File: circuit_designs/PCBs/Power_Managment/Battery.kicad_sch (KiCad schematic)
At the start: 20 parts, among them J1 Conn_01x02_Pin, J2 Conn_01x02_Pin, J3 Conn_01x02_Pin, U1 LM2596T-ADJ, U2 LM2596T-ADJ

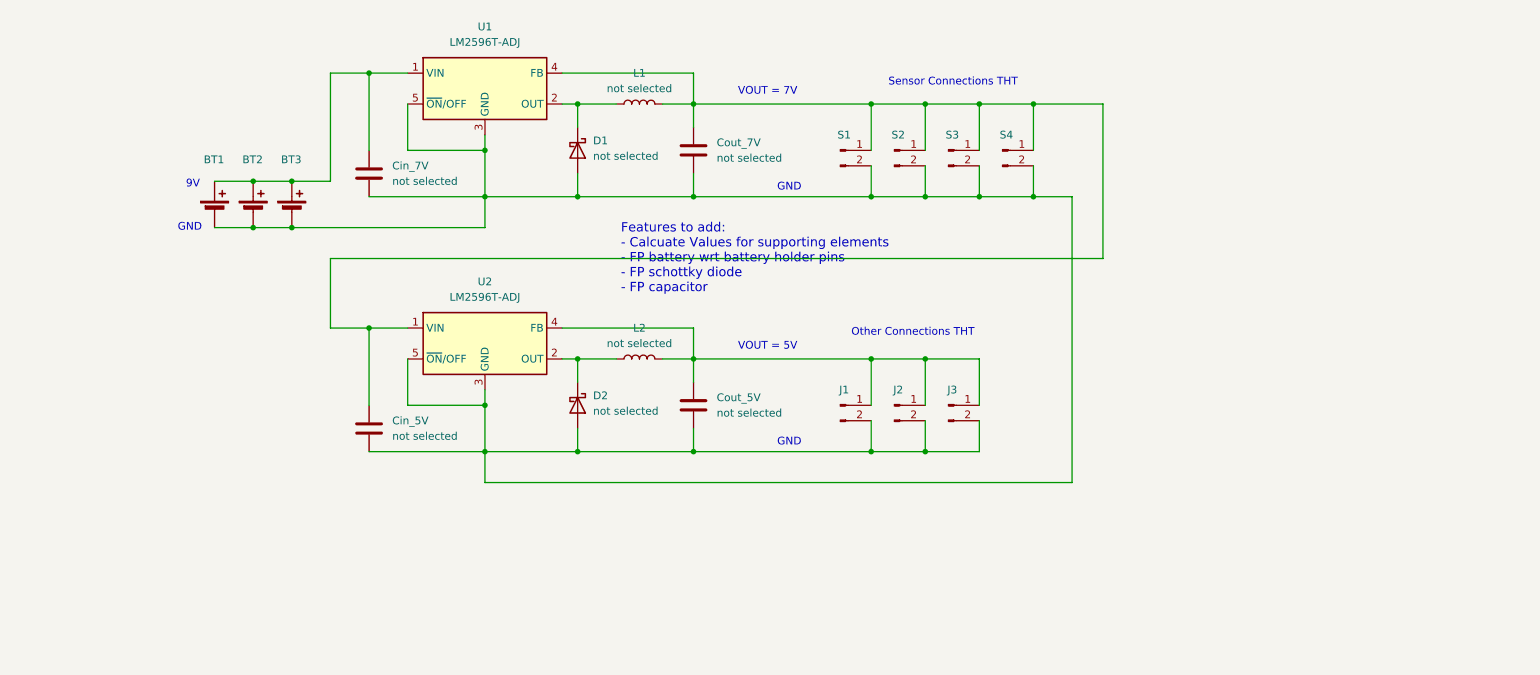
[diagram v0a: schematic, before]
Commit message: adam's and emmanuel's updates on the power management circuit - added values for the electronics (caps, inducts...) and added buzzer EPS
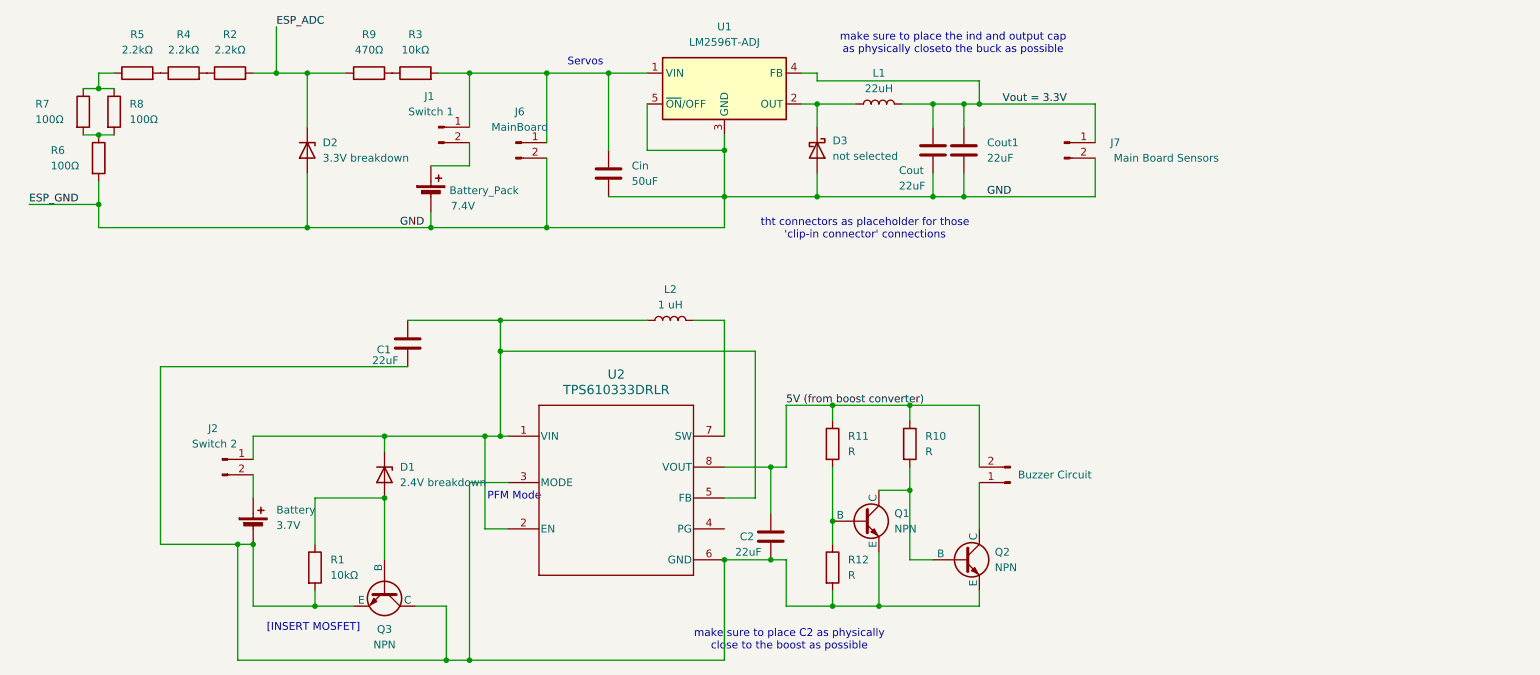
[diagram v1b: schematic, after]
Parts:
- removed BT1, BT2, BT3: 9V, symbol Device:Battery_Cell
- removed Cin_5V, Cin_7V, Cout_5V, Cout_7V: not selected, symbol Device:C
- removed D1, D2: not selected, symbol Device:D_Schottky
- removed S1, S2, S3, S4: Conn_01x02_Pin, mylibrary:External_Connection_2pin, symbol Connector:Conn_01x02_Pin
- removed U2: LM2596T-ADJ, Package_TO_SOT_THT:TO-220-5_P3.4x3.7mm_StaggerOdd_Lead3.8mm_Vertical, symbol Regulator_Switching:LM2596T-ADJ
- added Battery: 3.7V, symbol Device:Battery_Cell
- added Battery_Pack: 7.4V, symbol Device:Battery_Cell
- added C1, C2, Cout, Cout1: 22uF, symbol Device:C
- added Cin: 50uF, symbol Device:C
- added D1: 2.4V breakdown, Diode_THT:D_DO-41_SOD81_P10.16mm_Horizontal, symbol Diode:1N47xxA
- added D2: 3.3V breakdown, Diode_THT:D_DO-41_SOD81_P10.16mm_Horizontal, symbol Diode:1N47xxA
- added D3: not selected, symbol Device:D_Schottky
- added J6: MainBoard, symbol Connector:Conn_01x02_Pin
- added J7: Main Board Sensors, symbol Connector:Conn_01x02_Pin
- added Q1, Q2, Q3: NPN, symbol Simulation_SPICE:NPN
- added R1, R3: 10kΩ, symbol Device:R
- added R10, R11, R12: R, symbol Device:R
- added R2, R4, R5: 2.2kΩ, symbol Device:R
- added R6, R7, R8: 100Ω, symbol Device:R
- added R9: 470Ω, symbol Device:R
- added U2: TPS610333DRLR, mylibrary:TPS610333, symbol Project_Library:TPS610333DRLR
- J1: value Conn_01x02_Pin -> Switch 1; footprint mylibrary:External_Connection_2pin -> (none)
- J2: value Conn_01x02_Pin -> Switch 2; footprint mylibrary:External_Connection_2pin -> (none)
- J3: value Conn_01x02_Pin -> Buzzer Circuit; footprint mylibrary:External_Connection_2pin -> (none)
- L1: value not selected -> 22uH
- L2: value not selected -> 1 uH
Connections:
- net Vout = 3.3V: now reaches L1.2, U1.4 (FB)
- net Vout = 3.3V: now also Cout.1, Cout1.1, J7.1 (Pin_1)
- net at U1.1 (VIN): now also J1.1 (Pin_1), Cin.1, J6.1 (Pin_1), R3.2
- net at L2.1: now also J2.1 (Pin_1), C1.1, D1.1 (K), U2.1 (VIN), U2.2 (EN), U2.5 (FB)
- net at L1.1, U1.2 (OUT): now also D3.1 (K)
- new net: Battery.2 (-), C1.2, C2.2, Q1.3 (E), Q2.3 (E), Q3.1 (C), Q3.3 (E), R1.2, R12.2, U2.3 (MODE), U2.6 (GND)
- new net: L2.2, U2.7 (SW)
- new net: Battery_Pack.1 (+), J1.2 (Pin_2)
- new net: R4.1, R5.2
- new net: R2.1, R4.2
- new net: R5.1, R7.1, R8.1
- new net: R6.1, R7.2, R8.2
- new net: Battery.1 (+), J2.2 (Pin_2)
- new net: D1.2 (A), Q3.2 (B), R1.1
- new net: J3.1 (Pin_1), Q2.1 (C)
- new net: Q1.1 (C), Q2.2 (B), R10.2
- new net: Q1.2 (B), R11.2, R12.1
- new net: R3.1, R9.2
- new net 5V (from boost converter): C2.1, J3.2 (Pin_2), R10.1, R11.1, U2.8 (VOUT)
- new net ESP_ADC: D2.1 (K), R2.2, R9.1
- new net ESP_GND: Battery_Pack.2 (-), Cin.2, Cout.2, Cout1.2, D2.2 (A), D3.2 (A), J6.2 (Pin_2), J7.2 (Pin_2), R6.2, U1.3 (GND), U1.5 (~{ON}/OFF)
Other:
- note added: "PFM Mode"
- note added: "Servos"
- note added: "[INSERT MOSFET]"
- note added: "make sure to place C2 as physically close to the boost as possible"
- note added: "make sure to place the ind and output cap as physically closeto the buck as possible"
- note added: "tht connectors as placeholder for those 'clip-in connector' connections"
- note removed: "9V"
- note removed: "Features to add: - Calcuate Values for supporting elements - FP battery wrt battery holder pins - FP schottky diode - FP capacitor"
- note removed: "GND"
- note removed: "Other Connections THT"
- note removed: "Sensor Connections THT"
- note removed: "VOUT = 5V"
- note removed: "VOUT = 7V"

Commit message: thomas checked the power circuit
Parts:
- removed Q1, Q2: NPN, symbol Simulation_SPICE:NPN
- removed R10, R11, R12: R, symbol Device:R
- added Q4: PMOS, symbol Simulation_SPICE:NMOS
- added R13: 10kΩ, symbol Device:R
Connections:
- net at C1.1, L2.1, U2.1 (VIN)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: now also Q4.3 (S); no longer D1.1 (K), J2.1 (Pin_1)
- net at Battery.2 (-), C1.2, C2.2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: now also J3.1 (Pin_1), R13.2; no longer Q3.1 (C), Q3.3 (E)
- net 5V (from boost converter): no longer names the net of C2.1, J3.2 (Pin_2), U2.8 (VOUT)
- new net: Q3.3 (E), Q4.2 (G), R13.1
- new net: D1.1 (K), J2.1 (Pin_1), Q3.1 (C), Q4.1 (D)
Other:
- moved on the sheet: Battery, D1, J2, Q3, R1

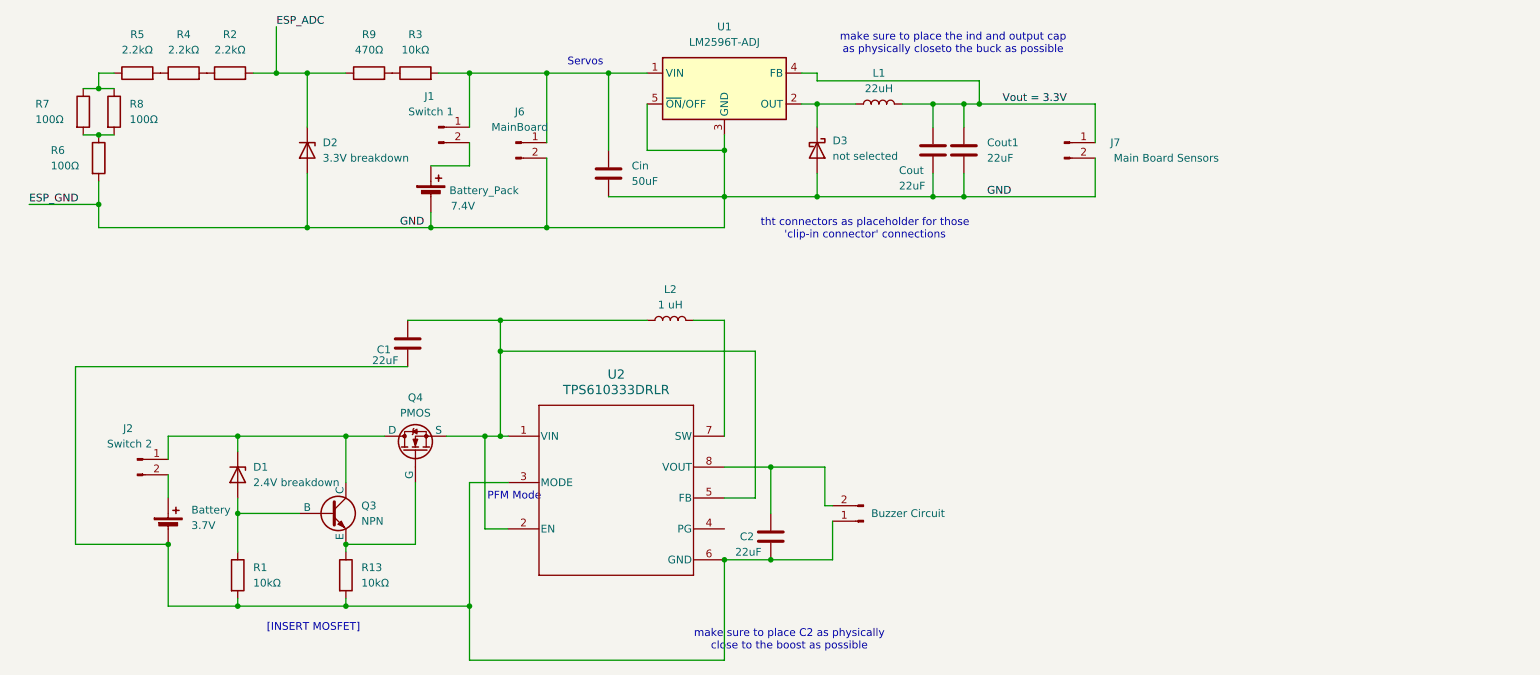
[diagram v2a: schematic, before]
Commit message: made power circuit into project and added buzzer circuit to it
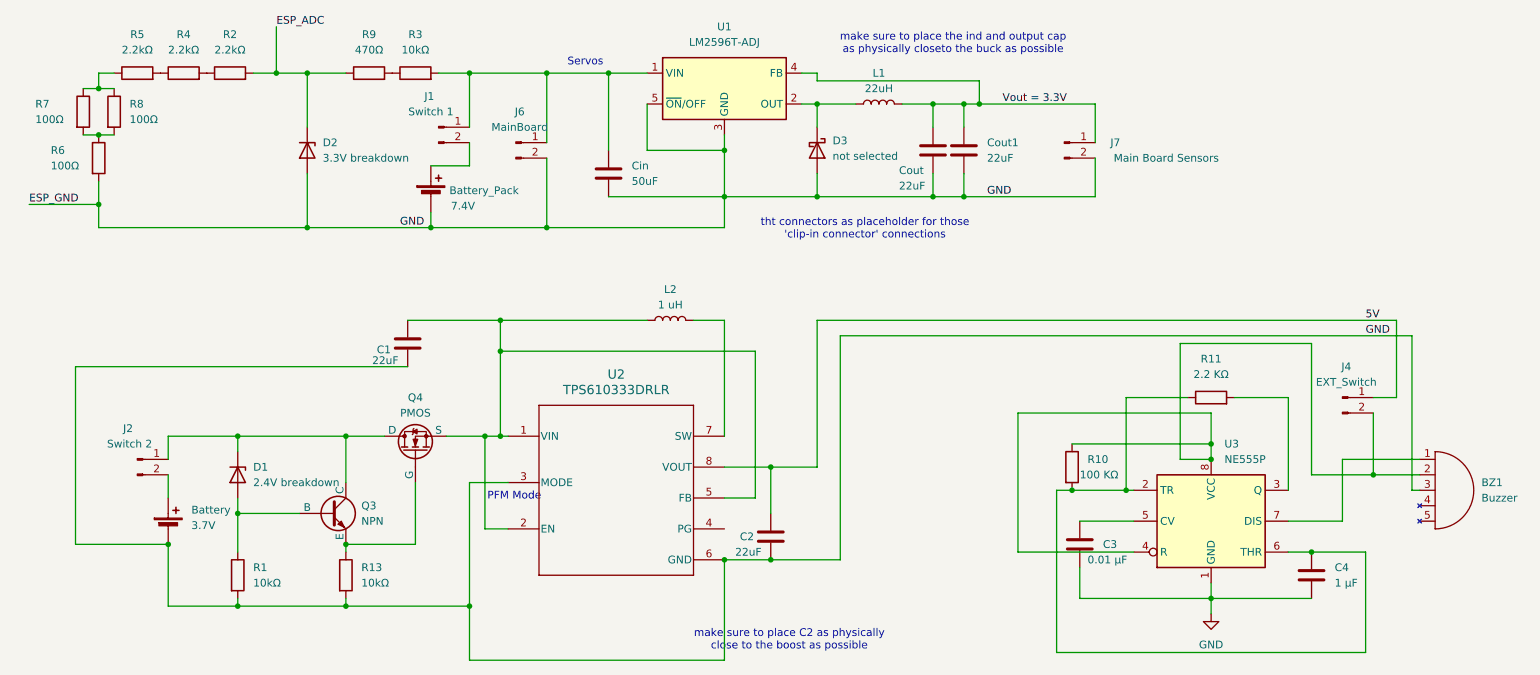
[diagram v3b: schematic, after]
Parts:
- removed J3: Buzzer Circuit, symbol Connector:Conn_01x02_Pin
- added BZ1: Buzzer, mylibrary:Buzzer_Connection, symbol Device:Buzzer
- added C3: 0.01 μF, Capacitor_THT:CP_Axial_L11.0mm_D5.0mm_P18.00mm_Horizontal, symbol Device:C
- added C4: 1 μF, Capacitor_THT:CP_Axial_L10.0mm_D6.0mm_P15.00mm_Horizontal, symbol Device:C
- added J4: EXT_Switch, mylibrary:External_Connection_2pin, symbol Connector:Conn_01x02_Pin
- added R10: 100 KΩ, Resistor_THT:R_Axial_DIN0207_L6.3mm_D2.5mm_P10.16mm_Horizontal, symbol Device:R
- added R11: 2.2 KΩ, Resistor_THT:R_Axial_DIN0207_L6.3mm_D2.5mm_P10.16mm_Horizontal, symbol Device:R
- added U3: NE555P, Package_DIP:DIP-8_W7.62mm, symbol Timer:NE555P
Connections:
- net ESP_GND is gone; now on net GND: Battery_Pack.2 (-), Cin.2, Cout.2, Cout1.2, D2.2 (A), D3.2 (A), J6.2 (Pin_2), J7.2 (Pin_2), R6.2, U1.3 (GND), U1.5 (~{ON}/OFF)
- net GND: now reaches Battery.2 (-), C1.2, C2.2, R1.2, R13.2, U2.3 (MODE), U2.6 (GND)
- net GND: now also BZ1.3 (G), C3.2, C4.2, U3.1 (GND)
- net 5V: now reaches C2.1, U2.8 (VOUT)
- net 5V: now also J4.1 (Pin_1)
- new net: BZ1.2 (5V), J4.2 (Pin_2), R10.1, U3.4 (R), U3.8 (VCC)
- new net: C3.1, U3.5 (CV)
- new net: C4.1, R10.2, R11.1, U3.2 (TR), U3.6 (THR)
- new net: BZ1.1 (Aux), U3.7 (DIS)
- new net: R11.2, U3.3 (Q)
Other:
- note removed: "[INSERT MOSFET]"

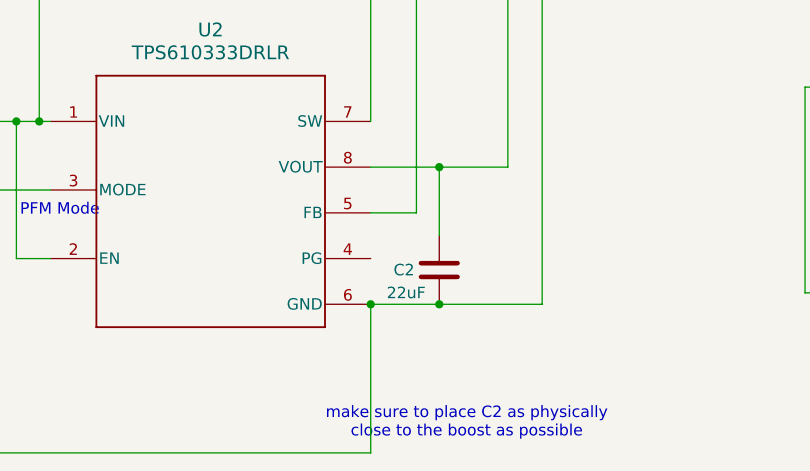
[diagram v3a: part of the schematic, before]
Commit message: tps610333 connected PG to GND
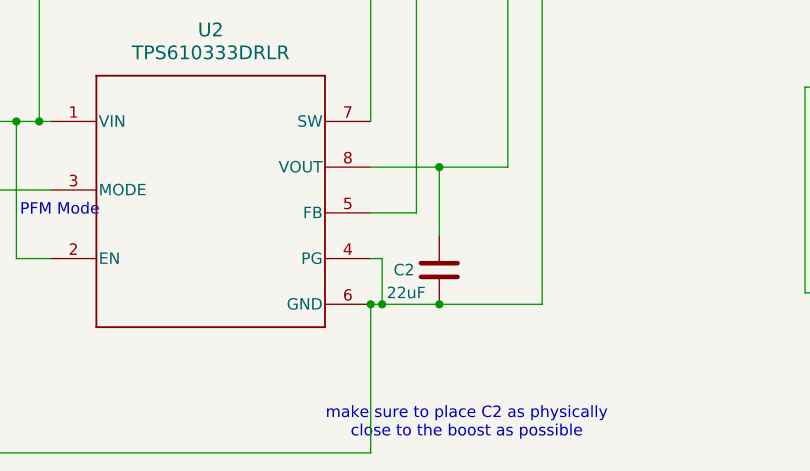
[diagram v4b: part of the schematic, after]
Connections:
- net GND: now also U2.4 (PG)
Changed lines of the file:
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@@
+	)
+	(junction
+		(at 132.08 144.78)
+		(diameter 0)
+		(color 0 0 0 0)
 	)
 	(junction
@@
 	(wire
 		(pts
+			(xy 130.81 139.7) (xy 132.08 139.7)
+		)
+		(stroke
+			(width 0)
+			(type default)
+		)
+	)
+	(wire
+		(pts
 			(xy 165.1 85.09) (xy 146.05 85.09)
 		)
@@
 	(wire
 		(pts
-			(xy 130.81 144.78) (xy 138.43 144.78)
+			(xy 130.81 144.78) (xy 132.08 144.78)
 		)
 		(stroke
@@
 	(wire
 		(pts
+			(xy 132.08 139.7) (xy 132.08 144.78)
+		)
+		(stroke
+			(width 0)
+			(type default)
+		)
+	)
+	(wire
+		(pts
 			(xy 205.74 109.22) (xy 227.33 109.22)
 		)
@@
 		)
 		(stroke
+			(width 0)
+			(type default)
+		)
+	)
+	(wire
+		(pts
+			(xy 132.08 144.78) (xy 138.43 144.78)
+		)
+		(stroke

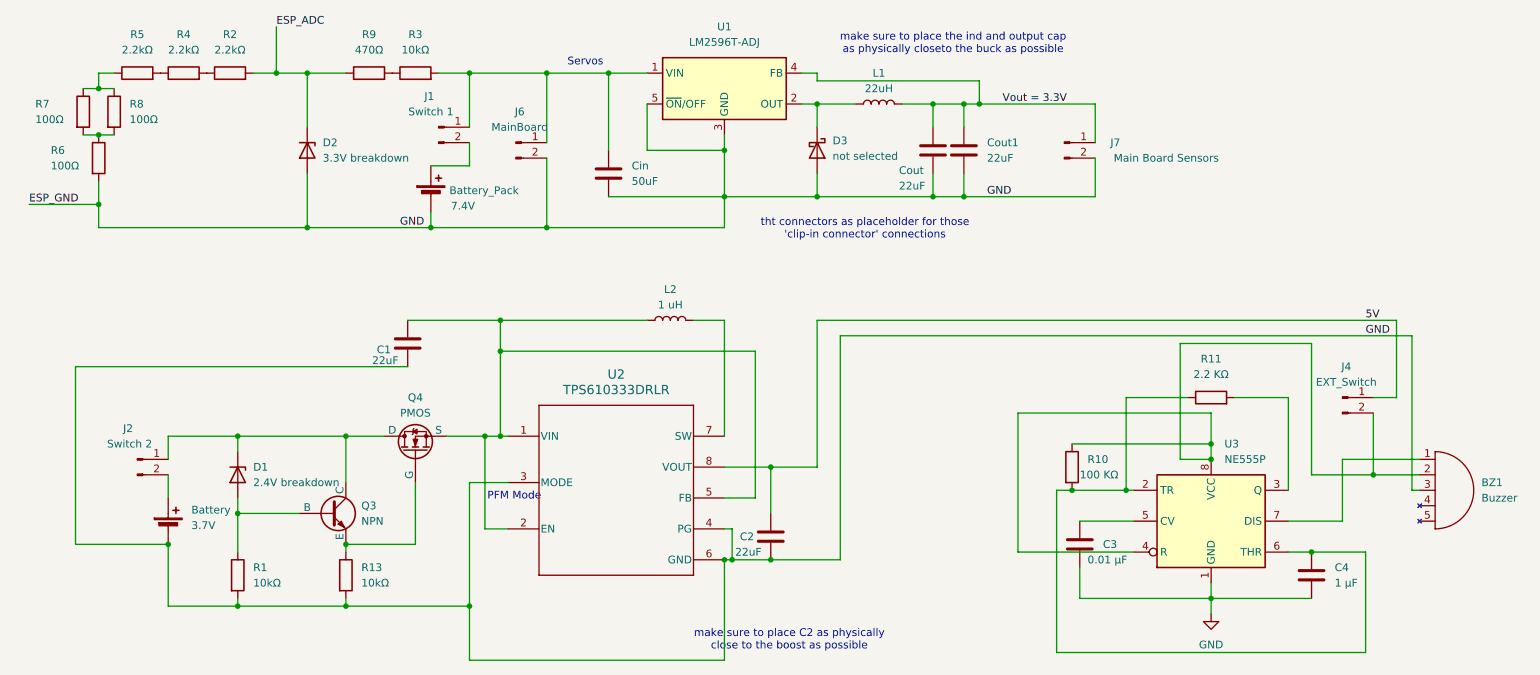
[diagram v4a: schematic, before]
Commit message: added most electrical componenets to the power circuit - missing bjt, pmos and zener for voltage proection circuit
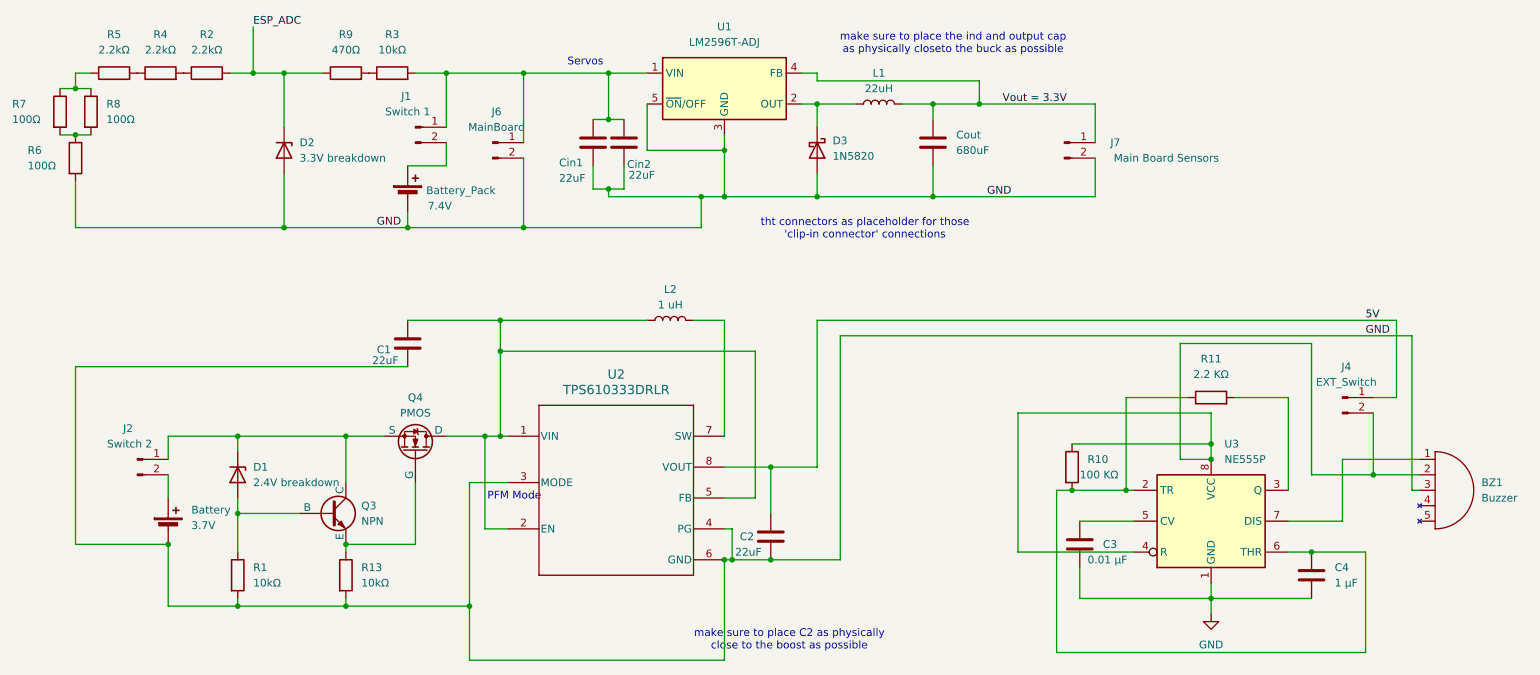
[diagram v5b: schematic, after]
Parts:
- removed Cin: 50uF, symbol Device:C
- removed Cout1: 22uF, symbol Device:C
- added Cin1, Cin2: 22uF, symbol Device:C
- Cout: value 22uF -> 680uF
- D3: value not selected -> 1N5820
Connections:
- net GND: now also Cin1.2, Cin2.2
- net at C1.1, L2.1, U2.1 (VIN)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: now also Q4.1 (D); no longer Q4.3 (S)
- net at J1.1 (Pin_1), J6.1 (Pin_1), R3.2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: now also Cin1.1, Cin2.1
- net at D1.1 (K), J2.1 (Pin_1), Q3.1 (C): now also Q4.3 (S); no longer Q4.1 (D)
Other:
- moved on the sheet: Battery_Pack, D2, J1, J6, Q4, R2, R3, R4, R5, R6, R7, R8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
